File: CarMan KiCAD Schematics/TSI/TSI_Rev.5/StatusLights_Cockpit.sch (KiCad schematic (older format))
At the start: 19 parts, among them Q3 ZVP1320F, U1 RDE03110S12, U11 TLP293, U13 TLP293

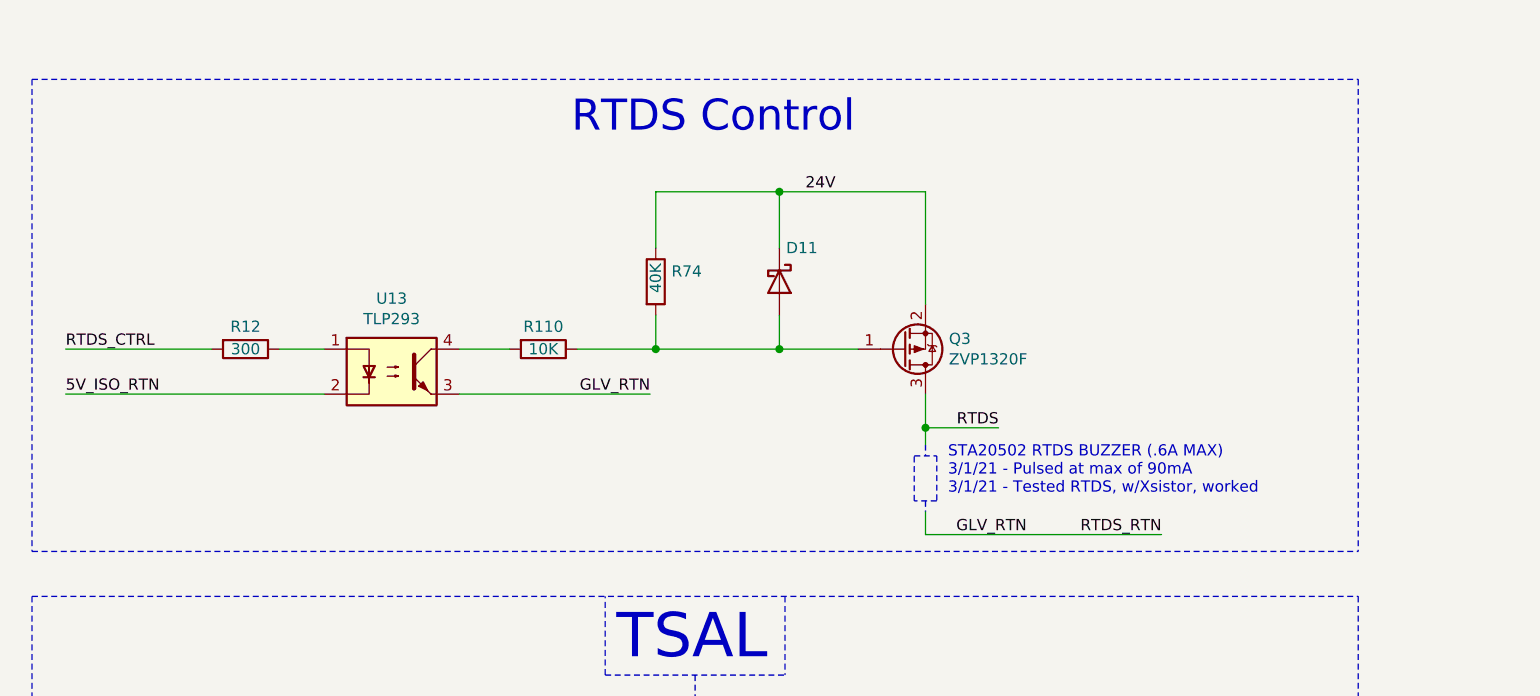
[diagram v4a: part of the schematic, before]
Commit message: Removed D11 (RTDS Zener diode), made RTDS sound warbled and trash
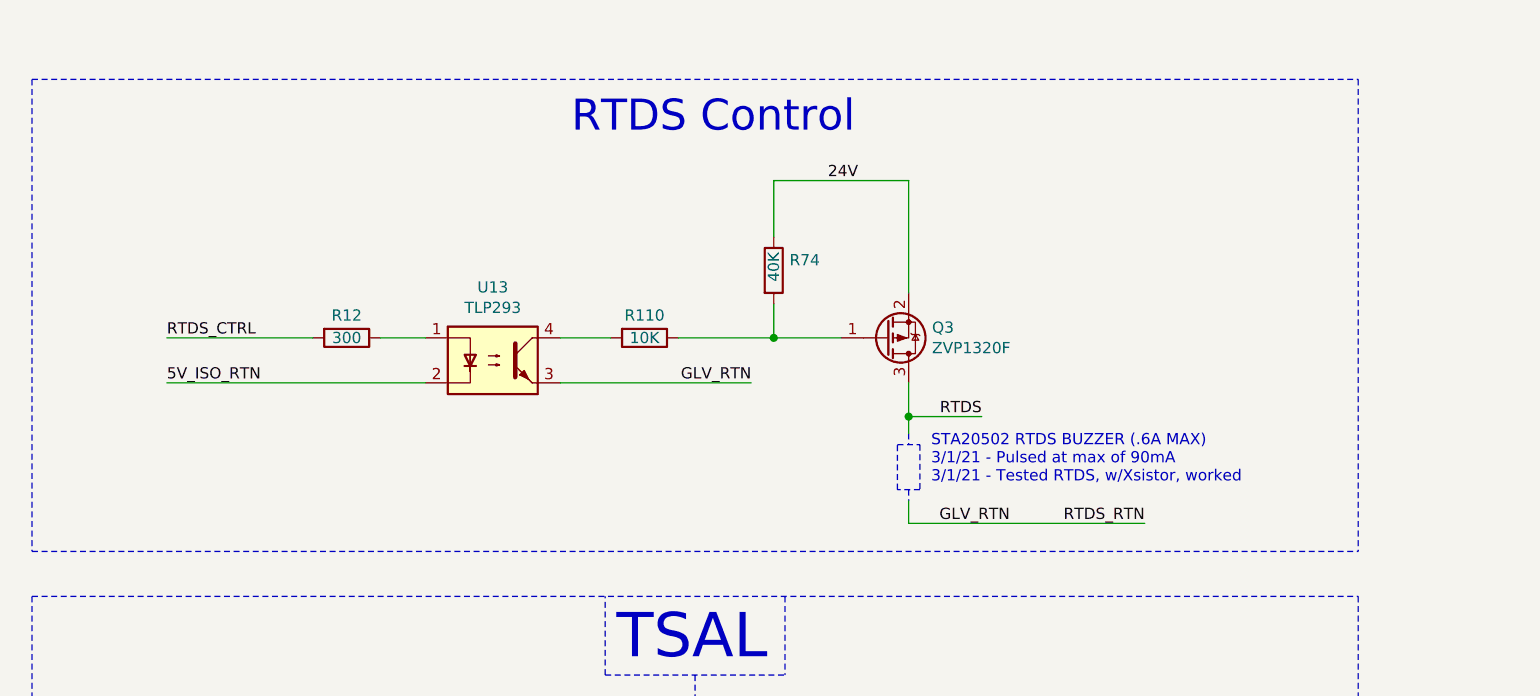
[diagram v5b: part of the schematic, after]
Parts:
- removed D11: MMSZ5231B-7-F, Diode_SMD:D_SOD-123, symbol CarMan_KiCAD_Library:D_Schottky
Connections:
- wire segments 86 -> 82
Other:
- moved on the sheet: Q3, R110, R12, R74, U13
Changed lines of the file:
@@
 Text Label 7675 3600 0    50   ~ 0
 D_LED_CTRL
-Text Label 4075 3450 2    50   ~ 0
+Text Label 4175 3400 2    50   ~ 0
 24V
 Text HLabel 800  5850 0    50   Input ~ 0
@@
 	-1   0    0    1
 $EndComp
-Connection ~ 3825 3450
-Wire Wire Line
-	3825 3450 4475 3450
-Wire Wire Line
-	3275 3450 3825 3450
-$Comp
-L CarMan_KiCAD_Library:D_Schottky D11
-U 1 1 5F9B6857
-P 3825 3850
-F 0 "D11" V 3675 3950 50  0000 C CNN
-F 1 "MMSZ5231B-7-F" H 3825 3976 50  0001 C CNN
-F 2 "Diode_SMD:D_SOD-123" H 3825 3850 50  0001 C CNN
-F 3 "~" H 3825 3850 50  0001 C CNN
-	1    3825 3850
-	0    1    1    0
-$EndComp
-Wire Wire Line
-	4475 4975 5525 4975
-Wire Wire Line
-	3825 4150 4175 4150
+Wire Wire Line
+	4400 4925 5450 4925
 $Comp
 L Device:Q_PMOS_GSD Q?
 U 1 1 5FC93215
-P 4375 4150
+P 4300 4100
 AR Path="/6196BF15/5FC93215" Ref="Q?"  Part="1"
 AR Path="/5FE1DCBA/5FC93215" Ref="Q3"  Part="1"
-F 0 "Q3" H 4579 4104 50  0000 L CNN
-F 1 "ZVP1320F" H 4579 4195 50  0000 L CNN
-F 2 "TSI_Rev_2021_Footprint_Lib:SOT23" H 4575 4250 50  0001 C CNN
-F 3 "https://www.snapeda.com/parts/ZVP1320FTA/Diodes%20Inc./datasheet/" H 4375 4150 50  0001 C CNN
-	1    4375 4150
+F 0 "Q3" H 4504 4054 50  0000 L CNN
+F 1 "ZVP1320F" H 4504 4145 50  0000 L CNN
+F 2 "TSI_Rev_2021_Footprint_Lib:SOT23" H 4500 4200 50  0001 C CNN
+F 3 "https://www.snapeda.com/parts/ZVP1320FTA/Diodes%20Inc./datasheet/" H 4300 4100 50  0001 C CNN
+	1    4300 4100
 	1    0    0    1
 $EndComp
 Wire Wire Line
-	1800 4150 1600 4150
-Text Notes 4575 4800 0    50   ~ 0
+	2250 4100 2050 4100
+Text Notes 4500 4750 0    50   ~ 0
 STA20502 RTDS BUZZER (.6A MAX)\n3/1/21 - Pulsed at max of 90mA\n3/1/21 - Tested RTDS, w/Xsistor, worked\n
 Wire Notes Line
-	4475 4825 4475 4875
-Wire Notes Line
-	4425 4625 4525 4625
-Wire Notes Line
-	4425 4825 4425 4625
-Wire Notes Line
-	4525 4825 4425 4825
-Wire Notes Line
-	4525 4625 4525 4825
-Wire Notes Line
-	4475 4575 4475 4625
-Text Label 4925 4975 2    50   ~ 0
+	4400 4775 4400 4825
+Wire Notes Line
+	4350 4575 4450 4575
+Wire Notes Line
+	4350 4775 4350 4575
+Wire Notes Line
+	4450 4775 4350 4775
+Wire Notes Line
+	4450 4575 4450 4775
+Wire Notes Line
+	4400 4525 4400 4575
+Text Label 4850 4925 2    50   ~ 0
 GLV_RTN
-Text Label 5525 4975 2    50   ~ 0
+Text Label 5450 4925 2    50   ~ 0
 RTDS_RTN
-Text Label 4800 4500 2    50   ~ 0
+Text Label 4725 4450 2    50   ~ 0
 RTDS
 Wire Wire Line
-	4475 4350 4475 4500
-Connection ~ 3825 4150
-Wire Wire Line
-	4475 3450 4475 3950
-Text Label 3250 4350 2    50   ~ 0
+	4400 4300 4400 4450
+Wire Wire Line
+	4400 3400 4400 3900
+Text Label 3700 4300 2    50   ~ 0
 GLV_RTN
 $Comp
 L TSI_Rev.5-rescue:TLP293-CarMan_KiCAD_Library-TSI_Rev.5-rescue U13
 U 1 1 5F9B7294
-P 2100 4250
-F 0 "U13" H 2100 4575 50  0000 C CNN
-F 1 "TLP293" H 2100 4484 50  0000 C CNN
-F 2 "Package_SO:SOIC-4_4.55x2.6mm_P1.27mm" H 1900 4050 50  0001 L CIN
-F 3 "" H 2100 4250 50  0001 L CNN
-	1    2100 4250
-	1    0    0    -1
-$EndComp
-Wire Wire Line
-	3825 3700 3825 3450
-Wire Wire Line
-	3275 3700 3275 3450
-Connection ~ 3275 4150
-Wire Wire Line
-	3825 4150 3825 4000
-Wire Wire Line
-	3275 4150 3825 4150
-Wire Wire Line
-	3275 4150 3275 4000
-Wire Wire Line
-	2925 4150 3275 4150
+P 2550 4200
+F 0 "U13" H 2550 4525 50  0000 C CNN
+F 1 "TLP293" H 2550 4434 50  0000 C CNN
+F 2 "Package_SO:SOIC-4_4.55x2.6mm_P1.27mm" H 2350 4000 50  0001 L CIN
+F 3 "" H 2550 4200 50  0001 L CNN
+	1    2550 4200
+	1    0    0    -1
+$EndComp
+Wire Wire Line
+	3800 3650 3800 3400
 $Comp
 L Device:R R74
 U 1 1 5F9BC6E2
-P 3275 3850
-F 0 "R74" H 3345 3896 50  0000 L CNN
-F 1 "40K" V 3275 3800 50  0000 L CNN
-F 2 "Resistor_SMD:R_0805_2012Metric_Pad1.15x1.40mm_HandSolder" V 3205 3850 50  0001 C CNN
-F 3 "~" H 3275 3850 50  0001 C CNN
-	1    3275 3850
+P 3800 3800
+F 0 "R74" H 3870 3846 50  0000 L CNN
+F 1 "40K" V 3800 3750 50  0000 L CNN
+F 2 "Resistor_SMD:R_0805_2012Metric_Pad1.15x1.40mm_HandSolder" V 3730 3800 50  0001 C CNN
+F 3 "~" H 3800 3800 50  0001 C CNN
+	1    3800 3800
 	1    0    0    -1
 $EndComp
@@
 L Device:R R110
 U 1 1 5F9BBE04
-P 2775 4150
-F 0 "R110" V 2675 4150 50  0000 C CNN
-F 1 "10K" V 2775 4150 50  0000 C CNN
-F 2 "Resistor_SMD:R_0805_2012Metric_Pad1.15x1.40mm_HandSolder" V 2705 4150 50  0001 C CNN
-F 3 "~" H 2775 4150 50  0001 C CNN
-	1    2775 4150
+P 3225 4100
+F 0 "R110" V 3125 4100 50  0000 C CNN
+F 1 "10K" V 3225 4100 50  0000 C CNN
+F 2 "Resistor_SMD:R_0805_2012Metric_Pad1.15x1.40mm_HandSolder" V 3155 4100 50  0001 C CNN
+F 3 "~" H 3225 4100 50  0001 C CNN
+	1    3225 4100
 	0    1    1    0
 $EndComp
-Text Label 650  4350 0    50   ~ 0
+Text Label 1100 4300 0    50   ~ 0
 5V_ISO_RTN
-Text Label 650  4150 0    50   ~ 0
+Text Label 1100 4100 0    50   ~ 0
 RTDS_CTRL
 $Comp
 L Device:R R12
 U 1 1 5F9BA8EE
-P 1450 4150
-F 0 "R12" V 1350 4150 50  0000 C CNN
-F 1 "300" V 1450 4150 50  0000 C CNN
-F 2 "Resistor_SMD:R_0805_2012Metric_Pad1.15x1.40mm_HandSolder" V 1380 4150 50  0001 C CNN
-F 3 "~" H 1450 4150 50  0001 C CNN
-	1    1450 4150
+P 1900 4100
+F 0 "R12" V 1800 4100 50  0000 C CNN
+F 1 "300" V 1900 4100 50  0000 C CNN
+F 2 "Resistor_SMD:R_0805_2012Metric_Pad1.15x1.40mm_HandSolder" V 1830 4100 50  0001 C CNN
+F 3 "~" H 1900 4100 50  0001 C CNN
+	1    1900 4100
 	0    1    1    0
 $EndComp
@@
 	500  500  2250 500
 Wire Wire Line
-	650  4150 1300 4150
-Wire Wire Line
-	650  4350 1800 4350
+	1100 4100 1750 4100
+Wire Wire Line
+	1100 4300 2250 4300
 Wire Wire Line
 	4400 7000 5000 7000
@@
 GLV_RTN
 Wire Wire Line
-	4475 4500 4475 4575
-Connection ~ 4475 4500
-Wire Wire Line
-	4475 4875 4475 4975
-Wire Wire Line
-	4475 4500 4800 4500
-Wire Wire Line
-	2400 4150 2625 4150
-Wire Wire Line
-	2400 4350 3250 4350
+	4400 4450 4400 4525
+Connection ~ 4400 4450
+Wire Wire Line
+	4400 4825 4400 4925
+Wire Wire Line
+	4400 4450 4725 4450
+Wire Wire Line
+	2850 4100 3075 4100
+Wire Wire Line
+	2850 4300 3700 4300
 Text HLabel 1150 1050 0    50   Input ~ 0
 5V_ISO_RTN
@@
 Wire Wire Line
 	8600 6200 8600 6050
+Wire Wire Line
+	3800 4100 3800 3950
+Wire Wire Line
+	4100 4100 3800 4100
+Wire Wire Line
+	3800 3400 4400 3400
+Wire Wire Line
+	3375 4100 3800 4100
+Connection ~ 3800 4100
 $EndSCHEMATC

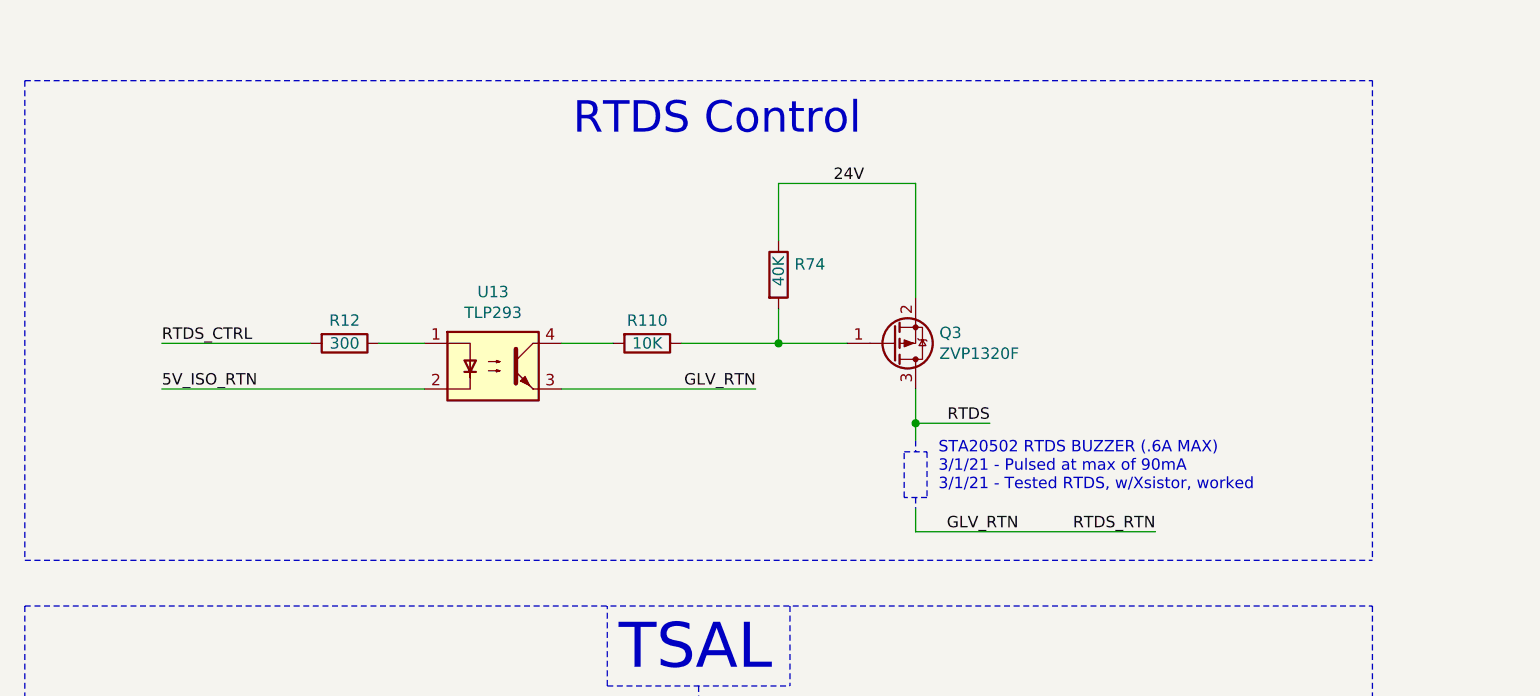
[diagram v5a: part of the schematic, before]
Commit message: Updated RTDS sound & added comments
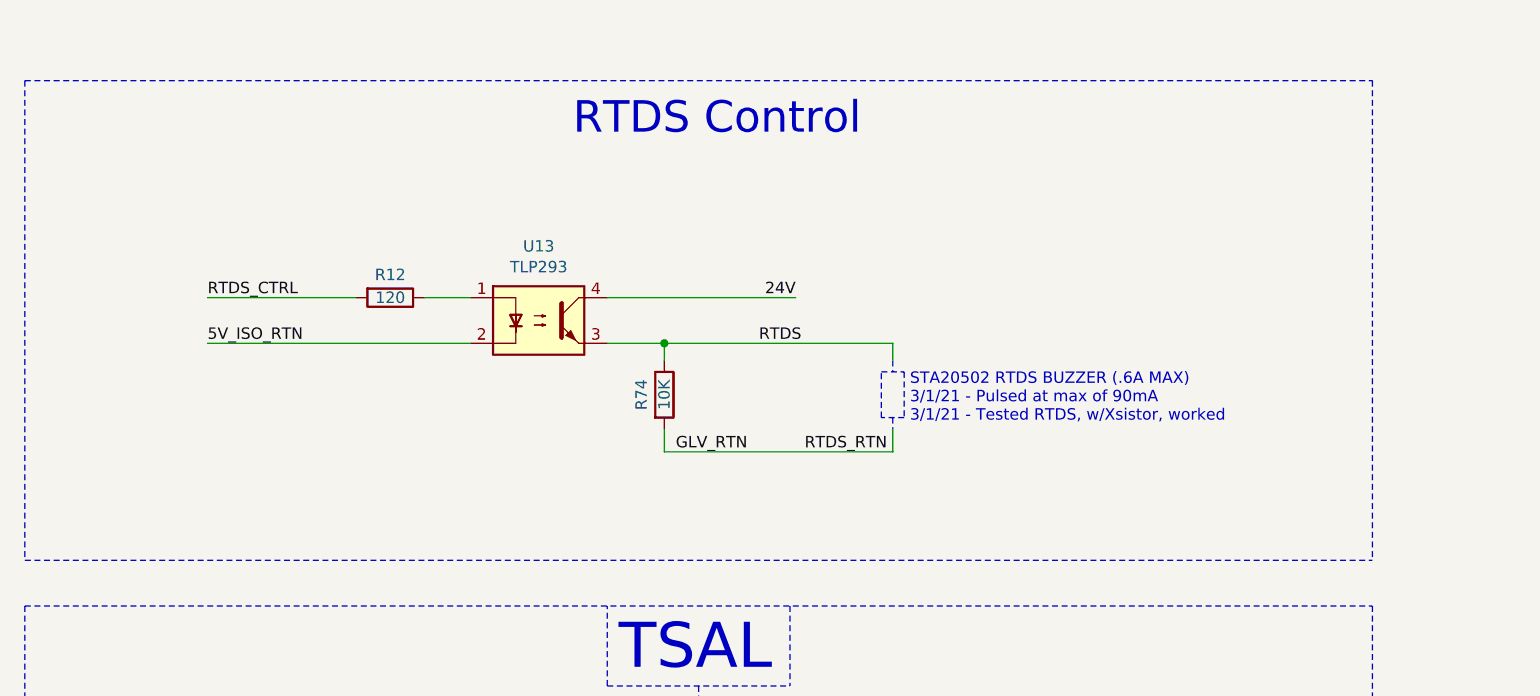
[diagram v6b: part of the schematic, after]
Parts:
- removed Q3: ZVP1320F, TSI_Rev_2021_Footprint_Lib:SOT23, symbol Device:Q_PMOS_GSD
- removed R74: 40K, Resistor_SMD:R_0805_2012Metric_Pad1.15x1.40mm_HandSolder, symbol Device:R
- R12: value 300 -> 120
- renumbered R110 to R74
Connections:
- wire segments 82 -> 77
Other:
- moved on the sheet: R12, R74, U13
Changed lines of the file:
@@
 Text Label 7675 3600 0    50   ~ 0
 D_LED_CTRL
-Text Label 4175 3400 2    50   ~ 0
+Text Label 3875 3900 2    50   ~ 0
 24V
 Text HLabel 800  5850 0    50   Input ~ 0
@@
 $EndComp
 Wire Wire Line
-	4400 4925 5450 4925
-$Comp
-L Device:Q_PMOS_GSD Q?
-U 1 1 5FC93215
-P 4300 4100
-AR Path="/6196BF15/5FC93215" Ref="Q?"  Part="1"
-AR Path="/5FE1DCBA/5FC93215" Ref="Q3"  Part="1"
-F 0 "Q3" H 4504 4054 50  0000 L CNN
-F 1 "ZVP1320F" H 4504 4145 50  0000 L CNN
-F 2 "TSI_Rev_2021_Footprint_Lib:SOT23" H 4500 4200 50  0001 C CNN
-F 3 "https://www.snapeda.com/parts/ZVP1320FTA/Diodes%20Inc./datasheet/" H 4300 4100 50  0001 C CNN
-	1    4300 4100
-	1    0    0    1
-$EndComp
-Wire Wire Line
-	2250 4100 2050 4100
-Text Notes 4500 4750 0    50   ~ 0
+	2450 3900 2250 3900
+Text Notes 4375 4450 0    50   ~ 0
 STA20502 RTDS BUZZER (.6A MAX)\n3/1/21 - Pulsed at max of 90mA\n3/1/21 - Tested RTDS, w/Xsistor, worked\n
 Wire Notes Line
-	4400 4775 4400 4825
-Wire Notes Line
-	4350 4575 4450 4575
-Wire Notes Line
-	4350 4775 4350 4575
-Wire Notes Line
-	4450 4775 4350 4775
-Wire Notes Line
-	4450 4575 4450 4775
-Wire Notes Line
-	4400 4525 4400 4575
-Text Label 4850 4925 2    50   ~ 0
+	4300 4425 4300 4475
+Wire Notes Line
+	4250 4225 4350 4225
+Wire Notes Line
+	4250 4425 4250 4225
+Wire Notes Line
+	4350 4425 4250 4425
+Wire Notes Line
+	4350 4225 4350 4425
+Wire Notes Line
+	4300 4175 4300 4225
+Text Label 3350 4575 0    50   ~ 0
 GLV_RTN
-Text Label 5450 4925 2    50   ~ 0
+Text Label 4275 4575 2    50   ~ 0
 RTDS_RTN
-Text Label 4725 4450 2    50   ~ 0
+Text Label 3900 4100 2    50   ~ 0
 RTDS
-Wire Wire Line
-	4400 4300 4400 4450
-Wire Wire Line
-	4400 3400 4400 3900
-Text Label 3700 4300 2    50   ~ 0
-GLV_RTN
 $Comp
 L TSI_Rev.5-rescue:TLP293-CarMan_KiCAD_Library-TSI_Rev.5-rescue U13
 U 1 1 5F9B7294
-P 2550 4200
-F 0 "U13" H 2550 4525 50  0000 C CNN
-F 1 "TLP293" H 2550 4434 50  0000 C CNN
-F 2 "Package_SO:SOIC-4_4.55x2.6mm_P1.27mm" H 2350 4000 50  0001 L CIN
-F 3 "" H 2550 4200 50  0001 L CNN
-	1    2550 4200
-	1    0    0    -1
-$EndComp
-Wire Wire Line
-	3800 3650 3800 3400
+P 2750 4000
+F 0 "U13" H 2750 4325 50  0000 C CNN
+F 1 "TLP293" H 2750 4234 50  0000 C CNN
+F 2 "Package_SO:SOIC-4_4.55x2.6mm_P1.27mm" H 2550 3800 50  0001 L CIN
+F 3 "" H 2750 4000 50  0001 L CNN
+	1    2750 4000
+	1    0    0    -1
+$EndComp
 $Comp
 L Device:R R74
-U 1 1 5F9BC6E2
-P 3800 3800
-F 0 "R74" H 3870 3846 50  0000 L CNN
-F 1 "40K" V 3800 3750 50  0000 L CNN
-F 2 "Resistor_SMD:R_0805_2012Metric_Pad1.15x1.40mm_HandSolder" V 3730 3800 50  0001 C CNN
-F 3 "~" H 3800 3800 50  0001 C CNN
-	1    3800 3800
-	1    0    0    -1
-$EndComp
-$Comp
-L Device:R R110
 U 1 1 5F9BBE04
-P 3225 4100
-F 0 "R110" V 3125 4100 50  0000 C CNN
-F 1 "10K" V 3225 4100 50  0000 C CNN
-F 2 "Resistor_SMD:R_0805_2012Metric_Pad1.15x1.40mm_HandSolder" V 3155 4100 50  0001 C CNN
-F 3 "~" H 3225 4100 50  0001 C CNN
-	1    3225 4100
-	0    1    1    0
-$EndComp
-Text Label 1100 4300 0    50   ~ 0
+P 3300 4325
+F 0 "R74" V 3200 4325 50  0000 C CNN
+F 1 "10K" V 3300 4325 50  0000 C CNN
+F 2 "Resistor_SMD:R_0805_2012Metric_Pad1.15x1.40mm_HandSolder" V 3230 4325 50  0001 C CNN
+F 3 "~" H 3300 4325 50  0001 C CNN
+	1    3300 4325
+	1    0    0    -1
+$EndComp
+Text Label 1300 4100 0    50   ~ 0
 5V_ISO_RTN
-Text Label 1100 4100 0    50   ~ 0
+Text Label 1300 3900 0    50   ~ 0
 RTDS_CTRL
 $Comp
 L Device:R R12
 U 1 1 5F9BA8EE
-P 1900 4100
-F 0 "R12" V 1800 4100 50  0000 C CNN
-F 1 "300" V 1900 4100 50  0000 C CNN
-F 2 "Resistor_SMD:R_0805_2012Metric_Pad1.15x1.40mm_HandSolder" V 1830 4100 50  0001 C CNN
-F 3 "~" H 1900 4100 50  0001 C CNN
-	1    1900 4100
+P 2100 3900
+F 0 "R12" V 2000 3900 50  0000 C CNN
+F 1 "120" V 2100 3900 50  0000 C CNN
+F 2 "Resistor_SMD:R_0805_2012Metric_Pad1.15x1.40mm_HandSolder" V 2030 3900 50  0001 C CNN
+F 3 "~" H 2100 3900 50  0001 C CNN
+	1    2100 3900
 	0    1    1    0
 $EndComp
@@
 	500  500  2250 500
 Wire Wire Line
-	1100 4100 1750 4100
-Wire Wire Line
-	1100 4300 2250 4300
+	1300 3900 1950 3900
+Wire Wire Line
+	1300 4100 2450 4100
 Wire Wire Line
 	4400 7000 5000 7000
@@
 Text Label 5600 7200 2    50   ~ 0
 GLV_RTN
-Wire Wire Line
-	4400 4450 4400 4525
-Connection ~ 4400 4450
-Wire Wire Line
-	4400 4825 4400 4925
-Wire Wire Line
-	4400 4450 4725 4450
-Wire Wire Line
-	2850 4100 3075 4100
-Wire Wire Line
-	2850 4300 3700 4300
 Text HLabel 1150 1050 0    50   Input ~ 0
 5V_ISO_RTN
@@
 	8600 6200 8600 6050
 Wire Wire Line
-	3800 4100 3800 3950
-Wire Wire Line
-	4100 4100 3800 4100
-Wire Wire Line
-	3800 3400 4400 3400
-Wire Wire Line
-	3375 4100 3800 4100
-Connection ~ 3800 4100
+	3050 3900 3875 3900
+Wire Wire Line
+	3050 4100 3300 4100
+Wire Wire Line
+	3300 4175 3300 4100
+Connection ~ 3300 4100
+Wire Wire Line
+	3300 4575 3300 4475
+Wire Wire Line
+	4300 4575 4300 4475
+Wire Wire Line
+	3300 4575 4300 4575
+Wire Wire Line
+	4300 4175 4300 4100
+Wire Wire Line
+	3300 4100 4300 4100
 $EndSCHEMATC
